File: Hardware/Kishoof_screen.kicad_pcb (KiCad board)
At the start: 2 copper layers, 41 x 41 mm, 5 parts, among them J1 Conn_01x02_Socket, J2 Conn_01x02_Socket, J3 Conn_01x02_Socket, J4 Conn_01x02_Socket

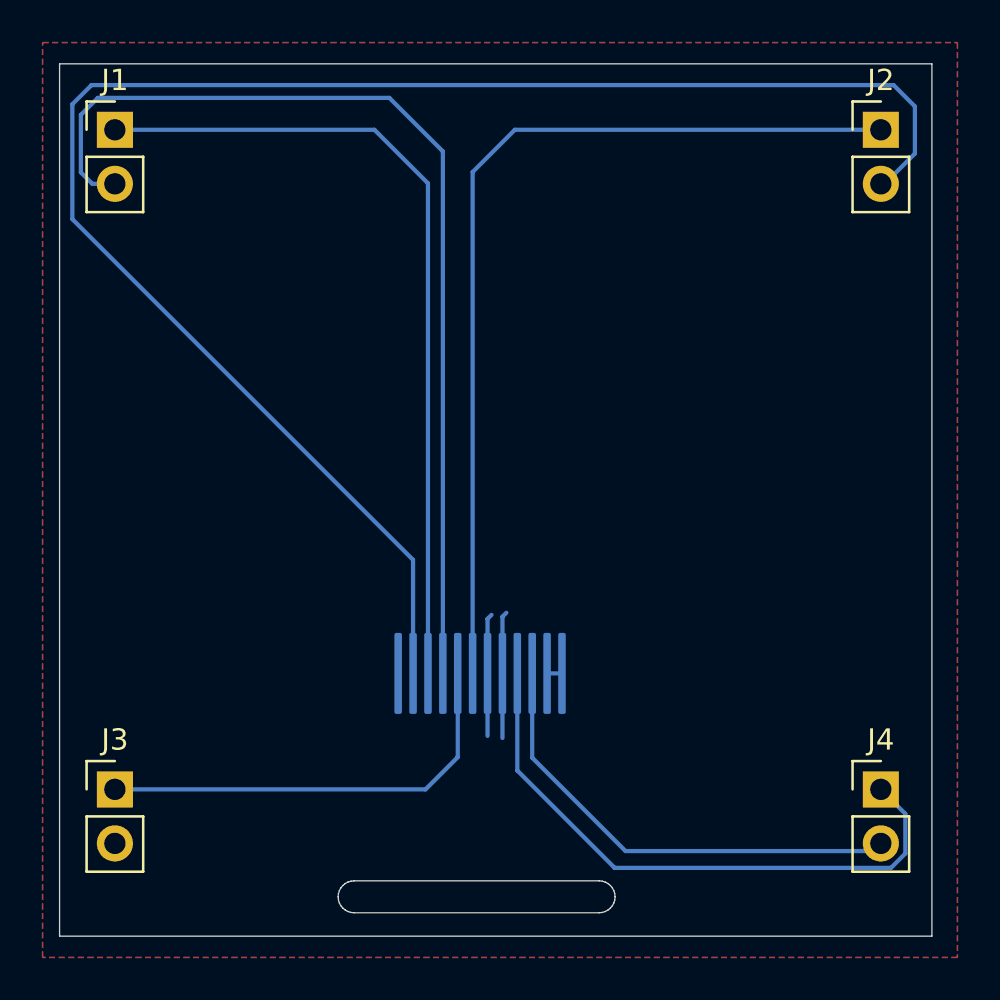
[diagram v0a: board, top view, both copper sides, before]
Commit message: Added STM32H7B0 project for testing
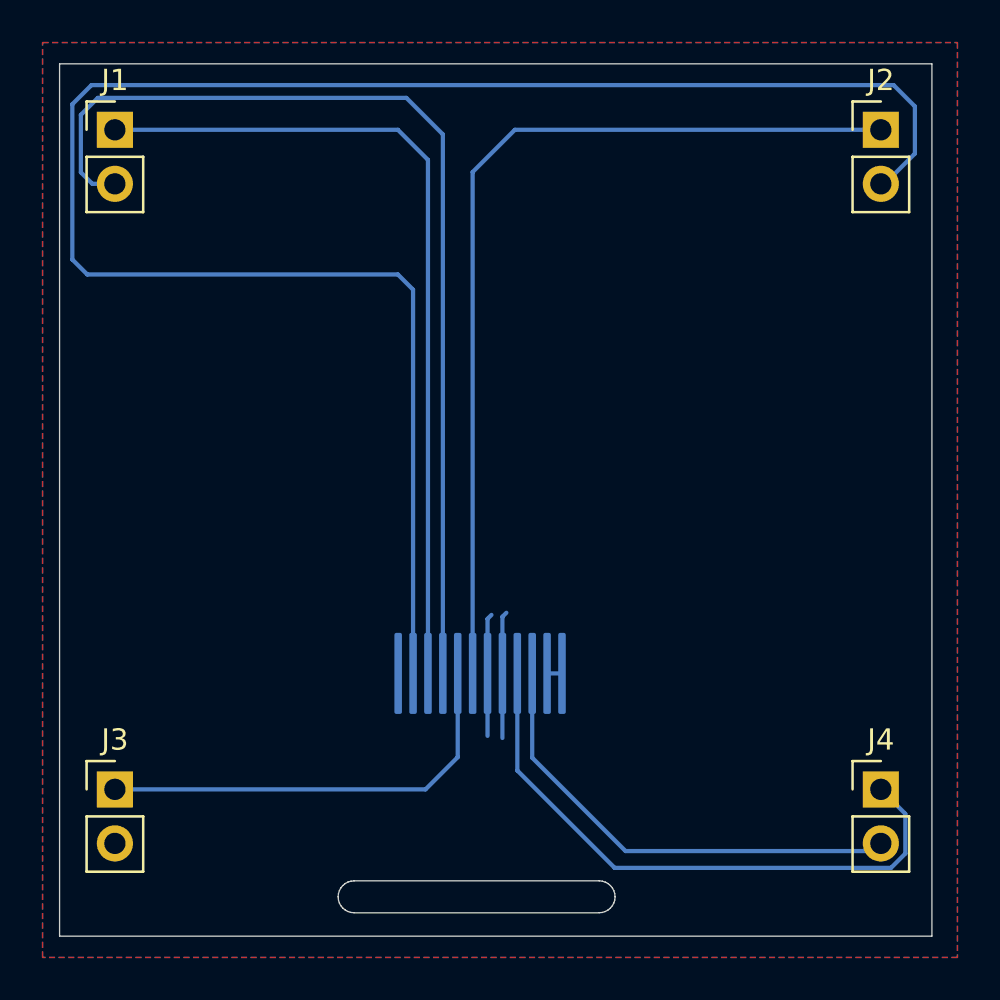
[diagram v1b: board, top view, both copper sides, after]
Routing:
- net /LCD_RESET: track 78.2 -> 86.7 mm
- net /LCD_SPI3_MOSI: track 38.8 -> 39.4 mm
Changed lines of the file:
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@@
 			(at 0 4.87 0)
 			(layer "F.Fab")
+			(hide yes)
 			(effects
 				(font
@@
 			(at 0 4.87 0)
 			(layer "F.Fab")
+			(hide yes)
 			(effects
 				(font
@@
 			(at 0 4.87 0)
 			(layer "F.Fab")
+			(hide yes)
 			(effects
 				(font
@@
 			(at 0 4.87 0)
 			(layer "F.Fab")
+			(hide yes)
 			(effects
 				(font
@@
 	)
 	(segment
-		(start 75.1139 45.6139)
+		(start 60.4 43.1)
+		(end 73.7 43.1)
+		(width 0.2)
+		(layer "B.Cu")
+		(net 1)
+	)
+	(segment
+		(start 75.1139 44.5139)
 		(end 75.1139 68.65)
 		(width 0.2)
@@
 	)
 	(segment
-		(start 72.6 43.1)
-		(end 75.1139 45.6139)
+		(start 73.7 43.1)
+		(end 75.1139 44.5139)
 		(width 0.2)
 		(layer "B.Cu")
@@
 	)
 	(segment
-		(start 60.4 43.1)
-		(end 72.6 43.1)
-		(width 0.2)
-		(layer "B.Cu")
-		(net 1)
+		(start 74.1 41.6)
+		(end 59.6 41.6)
+		(width 0.2)
+		(layer "B.Cu")
+		(net 2)
+	)
+	(segment
+		(start 75.8139 68.65)
+		(end 75.8139 43.3139)
+		(width 0.2)
+		(layer "B.Cu")
+		(net 2)
+	)
+	(segment
+		(start 58.8 45.1)
+		(end 59.34 45.64)
+		(width 0.2)
+		(layer "B.Cu")
+		(net 2)
+	)
+	(segment
+		(start 59.6 41.6)
+		(end 58.8 42.4)
+		(width 0.2)
+		(layer "B.Cu")
+		(net 2)
+	)
+	(segment
+		(start 75.8139 43.3139)
+		(end 74.1 41.6)
+		(width 0.2)
+		(layer "B.Cu")
+		(net 2)
+	)
+	(segment
+		(start 58.8 42.4)
+		(end 58.8 45.1)
+		(width 0.2)
+		(layer "B.Cu")
+		(net 2)
 	)
 	(segment
@@
 	)
 	(segment
-		(start 75.8139 44.1139)
-		(end 73.3 41.6)
-		(width 0.2)
-		(layer "B.Cu")
-		(net 2)
-	)
-	(segment
-		(start 58.8 42.4)
-		(end 58.8 45.1)
-		(width 0.2)
-		(layer "B.Cu")
-		(net 2)
-	)
-	(segment
-		(start 59.6 41.6)
-		(end 58.8 42.4)
-		(width 0.2)
-		(layer "B.Cu")
-		(net 2)
-	)
-	(segment
-		(start 73.3 41.6)
-		(end 59.6 41.6)
-		(width 0.2)
-		(layer "B.Cu")
-		(net 2)
-	)
-	(segment
-		(start 58.8 45.1)
-		(end 59.34 45.64)
-		(width 0.2)
-		(layer "B.Cu")
-		(net 2)
-	)
-	(segment
-		(start 75.8139 68.65)
-		(end 75.8139 44.1139)
-		(width 0.2)
-		(layer "B.Cu")
-		(net 2)
-	)
-	(segment
 		(start 96.4 43.1)
 		(end 79.2 43.1)
@@
 	)
 	(segment
+		(start 96.4 45.64)
+		(end 96.58 45.64)
+		(width 0.2)
+		(layer "B.Cu")
+		(net 4)
+	)
+	(segment
+		(start 97 41)
+		(end 59.3 41)
+		(width 0.2)
+		(layer "B.Cu")
+		(net 4)
+	)
+	(segment
+		(start 98 44.22)
+		(end 98 42)
+		(width 0.2)
+		(layer "B.Cu")
+		(net 4)
+	)
+	(segment
+		(start 58.4 49.2)
+		(end 59.1 49.9)
+		(width 0.2)
+		(layer "B.Cu")
+		(net 4)
+	)
+	(segment
+		(start 58.4 41.9)
+		(end 58.4 49.2)
+		(width 0.2)
+		(layer "B.Cu")
+		(net 4)
+	)
+	(segment
+		(start 59.1 49.9)
+		(end 73.7 49.9)
+		(width 0.2)
+		(layer "B.Cu")
+		(net 4)
+	)
+	(segment
 		(start 59.3 41)
 		(end 58.4 41.9)
@@
 	)
 	(segment
-		(start 74.4139 63.3139)
+		(start 96.58 45.64)
+		(end 98 44.22)
+		(width 0.2)
+		(layer "B.Cu")
+		(net 4)
+	)
+	(segment
+		(start 74.4139 50.6139)
 		(end 74.4139 68.65)
 		(width 0.2)
@@
 	)
 	(segment
-		(start 58.4 41.9)
-		(end 58.4 47.3)
-		(width 0.2)
-		(layer "B.Cu")
-		(net 4)
-	)
-	(segment
-		(start 96.4 45.64)
-		(end 96.58 45.64)
-		(width 0.2)
-		(layer "B.Cu")
-		(net 4)
-	)
-	(segment
-		(start 97 41)
-		(end 59.3 41)
-		(width 0.2)
-		(layer "B.Cu")
-		(net 4)
-	)
-	(segment
-		(start 58.4 47.3)
-		(end 74.4139 63.3139)
-		(width 0.2)
-		(layer "B.Cu")
-		(net 4)
-	)
-	(segment
-		(start 98 44.22)
-		(end 98 42)
+		(start 73.7 49.9)
+		(end 74.4139 50.6139)
 		(width 0.2)
 		(layer "B.Cu")
@@
 		(width 0.2)
 		(layer "B.Cu")
-		(net 4)
-	)
-	(segment
-		(start 96.58 45.64)
-		(end 98 44.22)
-		(width 0.2)
-		(layer "B.Cu")

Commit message: Control board routed; updated lcd riser
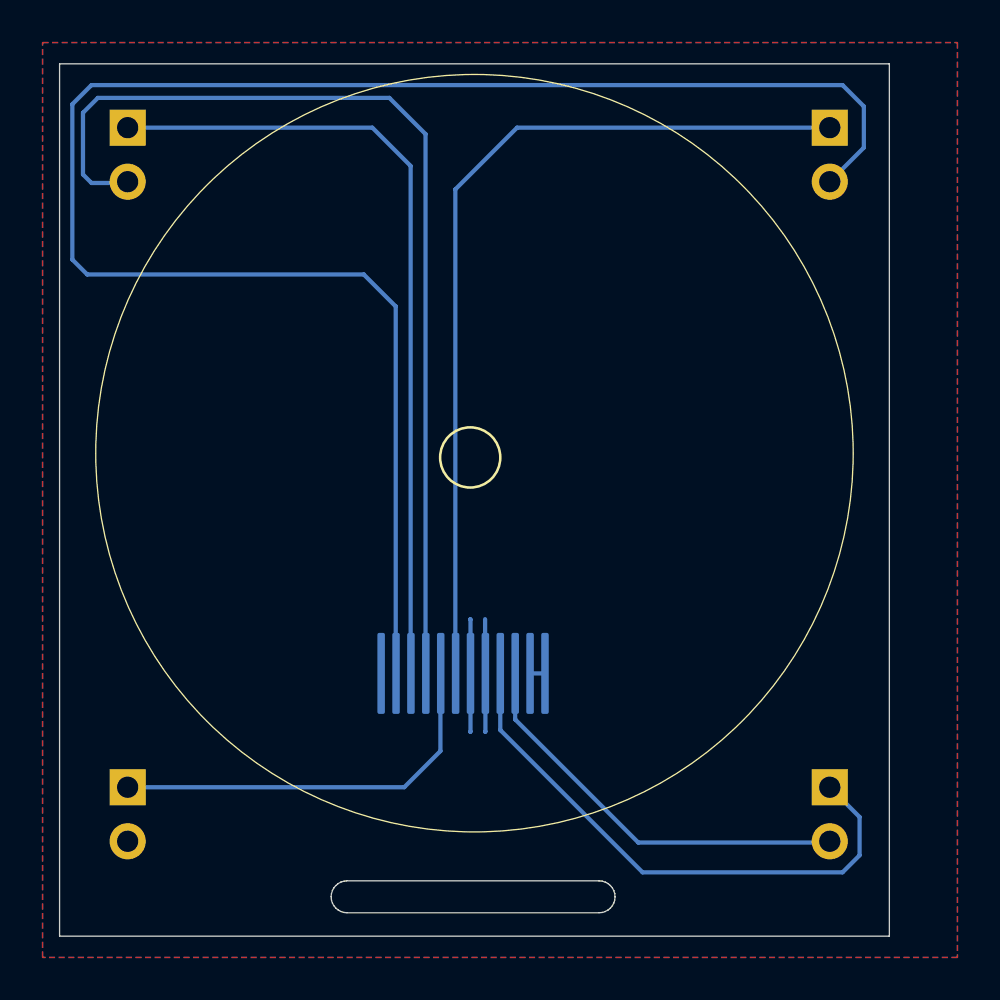
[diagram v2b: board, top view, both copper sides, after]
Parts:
- added REF**: 3D_Dummy, Custom_Footprints:3D_Dummy, F.Cu at (77.1, 58.5)
- J1, J2, J3, J4: moved to B.Cu
- moved J2 2.40 mm to (94.0, 43.0), turned to 180 degrees
- moved J4 2.40 mm to (94.0, 74.0), turned to 180 degrees
- moved U1 0.80 mm to (80.6, 68.7)
- moved J1 0.61 mm to (61.0, 43.0), turned to 180 degrees
- moved J3 0.61 mm to (61.0, 74.0), turned to 180 degrees
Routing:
- net /LCD_RESET: track 86.7 -> 83.0 mm
- net /LCD_BACKLIGHT: track 22.3 -> 19.5 mm
- net +3.3V: track 28.5 -> 26.4 mm
- net /LCD_DC: track 43.6 -> 41.6 mm
- net /LCD_SPI3_SS: track 20.7 -> 19.1 mm
- net /LCD_SPI3_MOSI: track 39.4 -> 37.9 mm
- net GND: track 12.4 -> 11.3 mm
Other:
- board size 41 x 41 mm -> 39 x 41 mm

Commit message: PCBs v1.0 ordered
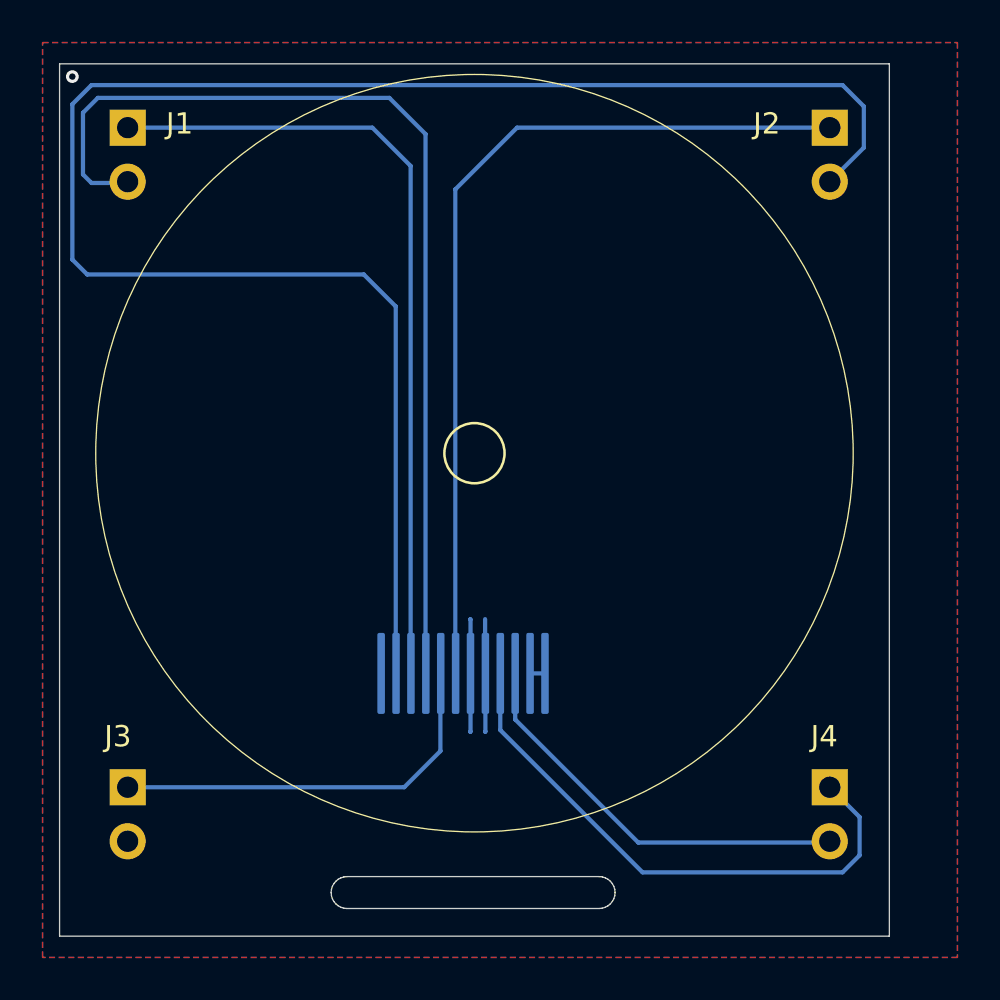
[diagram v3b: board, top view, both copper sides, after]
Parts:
- moved REF** 0.28 mm to (77.3, 58.3)
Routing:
- net GND: vias 0 -> 1
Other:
- outline, holes or cut-outs redrawn
- board text added: "J1"
- board text added: "J2"
- board text added: "J3"
- board text added: "J4"
- board text added: "Mountjoy Modular 2024 Kishoof LCD Riser v1.0"
